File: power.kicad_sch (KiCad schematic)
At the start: 17 parts, among them Q3 AO3401A, SW2 SW_On_Off, U1 MCP73831-2-MC, U3 TPS61200DRC

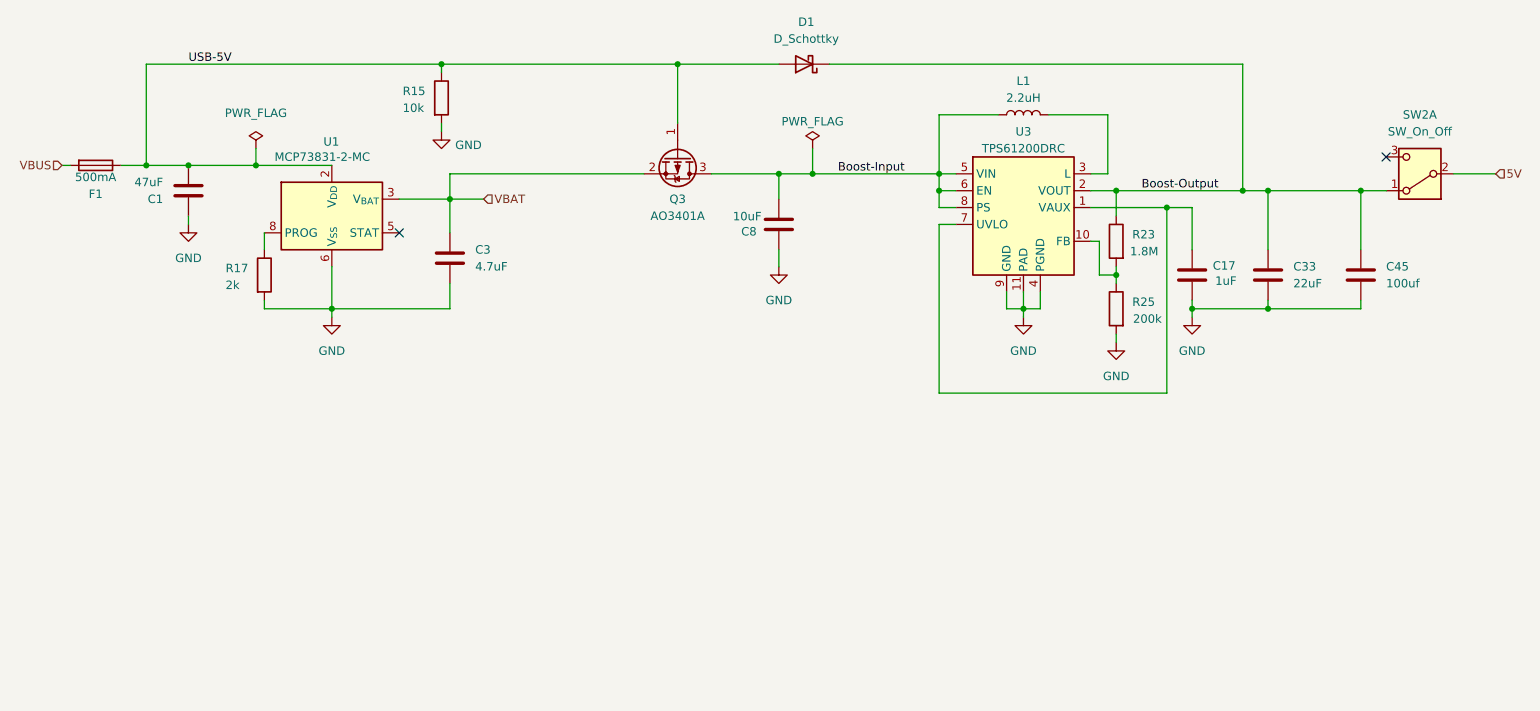
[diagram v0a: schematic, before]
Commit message: switched oout led footprint
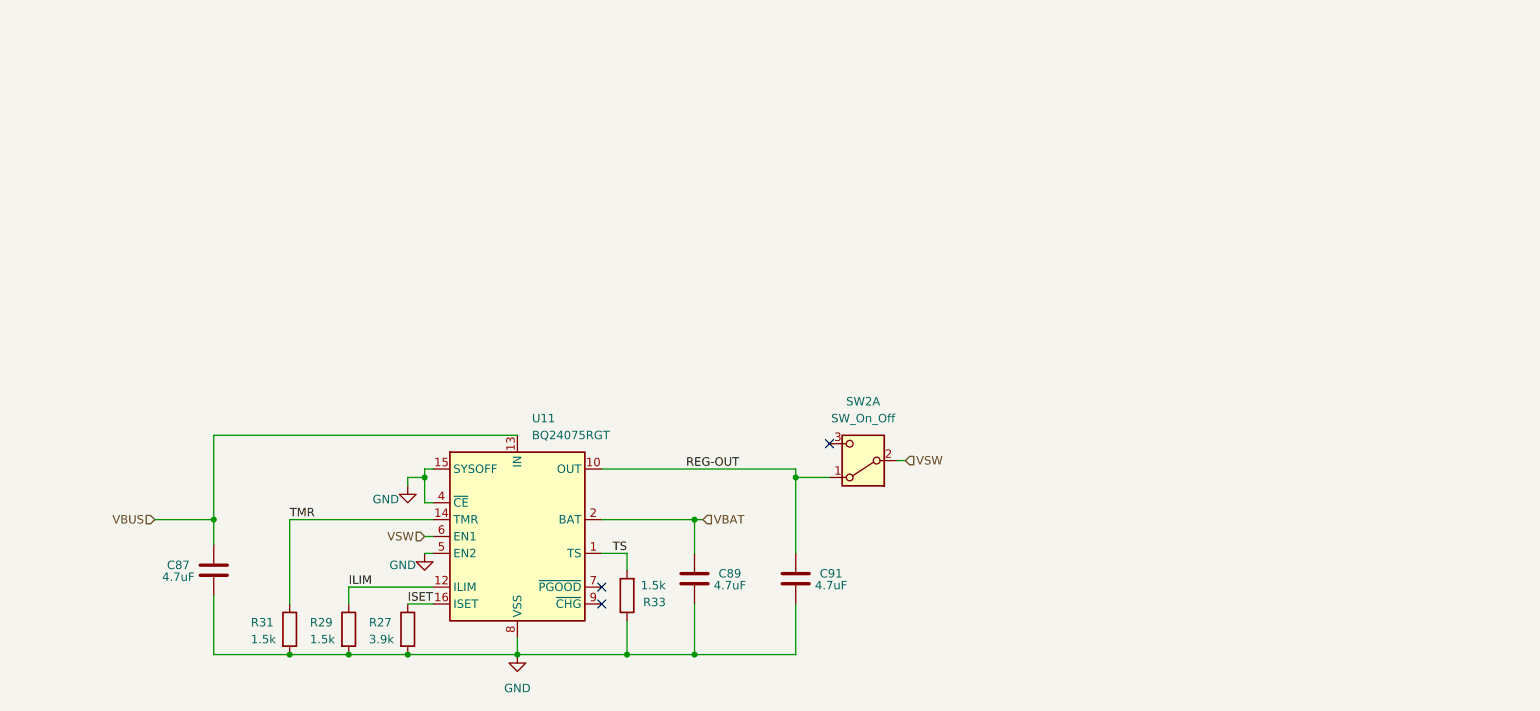
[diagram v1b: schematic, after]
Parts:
- removed C1: 47uF, Capacitor_SMD:C_0603_1608Metric, symbol Device:C
- removed C17: 1uF, Capacitor_SMD:C_0402_1005Metric, symbol Device:C
- removed C3: 4.7uF, Capacitor_SMD:C_0603_1608Metric, symbol Device:C
- removed C33: 22uF, Capacitor_SMD:C_0603_1608Metric, symbol Device:C
- removed C45: 100uf, Capacitor_SMD:C_0805_2012Metric, symbol Device:C
- removed C8: 10uF, Capacitor_SMD:C_0603_1608Metric, symbol Device:C
- removed D1: D_Schottky, Diode_SMD:D_SOD-123, symbol Device:D_Schottky
- removed F1: 500mA, Fuse:Fuse_0603_1608Metric, symbol Device:Fuse
- removed L1: 2.2uH, LPS3015-222MRC:IND_LPS3015-222MRC, symbol Device:L
- removed Q3: AO3401A, Package_TO_SOT_SMD:SOT-23, symbol Transistor_FET:AO3401A
- removed R15: 10k, Resistor_SMD:R_0402_1005Metric, symbol Device:R
- removed R17: 2k, Resistor_SMD:R_0402_1005Metric, symbol Device:R
- removed R23: 1.8M, Resistor_SMD:R_0402_1005Metric, symbol Device:R
- removed R25: 200k, Resistor_SMD:R_0402_1005Metric, symbol Device:R
- removed U1: MCP73831-2-MC, Package_DFN_QFN:DFN-8-1EP_3x2mm_P0.5mm_EP1.7x1.4mm, symbol Battery_Management:MCP73831-2-MC
- removed U3: TPS61200DRC, Package_SON:Texas_S-PVSON-N10_ThermalVias, symbol Regulator_Switching:TPS61200DRC
- added C87, C89, C91: 4.7uF, Capacitor_SMD:C_0402_1005Metric, symbol Device:C
- added R27: 3.9k, Resistor_SMD:R_0402_1005Metric, symbol Device:R
- added R29, R31, R33: 1.5k, Resistor_SMD:R_0402_1005Metric, symbol Device:R
- added U11: BQ24075RGT, Package_DFN_QFN:VQFN-16-1EP_3x3mm_P0.5mm_EP1.6x1.6mm, symbol Battery_Management:BQ24075RGT
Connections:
- net GND: now also C87.1, C89.1, C91.1, R27.2, R29.2, R31.2, R33.1, U11.15 (SYSOFF), U11.17 (VSS), U11.4 (~{CE}), U11.5 (EN2), U11.8 (VSS)
- net VBAT: now also C89.2, U11.2 (BAT), U11.3 (BAT)
- net VBUS: now also C87.2, U11.13 (IN)
- net 5V renamed VSW
- net VSW: now also U11.6 (EN1)
- net Boost-Output renamed REG-OUT
- net REG-OUT: now also C91.2, U11.10 (OUT), U11.11 (OUT)
- new net ILIM: R29.1, U11.12 (ILIM)
- new net ISET: R27.1, U11.16 (ISET)
- new net TMR: R31.1, U11.14 (TMR)
- new net TS: R33.2, U11.1 (TS)
- no-connect marks 2 -> 3
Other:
- moved on the sheet: SW2A

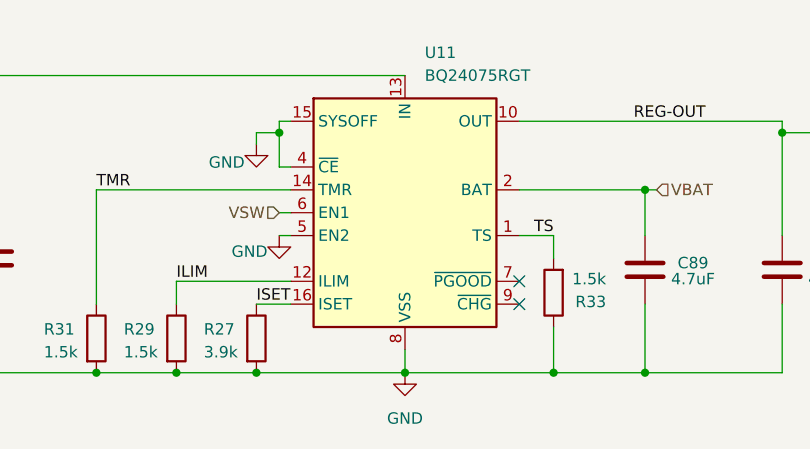
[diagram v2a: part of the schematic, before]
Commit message: added lcsc part numbers
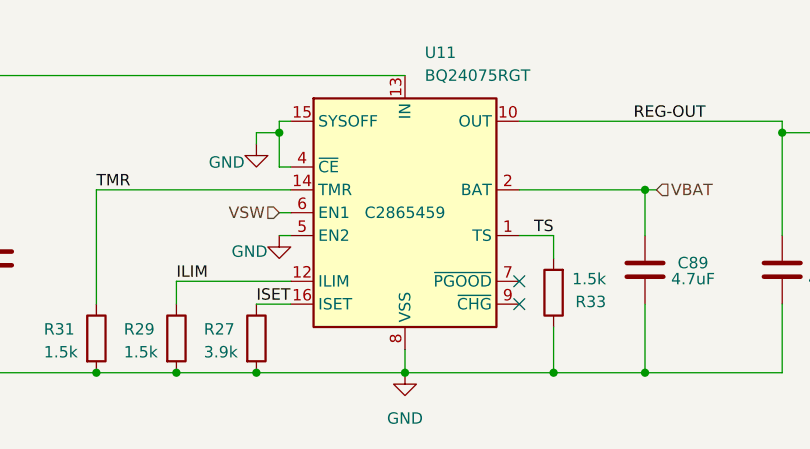
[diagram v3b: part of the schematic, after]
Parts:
- C87, C89, C91: LCSC (none) -> C307423
- R27: LCSC (none) -> C131467
- R29, R31, R33: LCSC (none) -> C25867
- U11: LCSC (none) -> C2865459
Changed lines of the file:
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@@
+			)
+		)
+		(property "LCSC" "C2865459"
+			(at 105.41 144.78 0)
+			(effects
+				(font
+					(size 1.27 1.27)
+				)
 			)
 		)
@@
 			)
 		)
+		(property "LCSC" "C307423"
+			(at 147.32 151.13 0)
+			(effects
+				(font
+					(size 1.27 1.27)
+				)
+				(hide yes)
+			)
+		)
 		(pin "1"
 		)
@@
 			)
 		)
+		(property "LCSC" "C25867"
+			(at 80.01 158.75 0)
+			(effects
+				(font
+					(size 1.27 1.27)
+				)
+				(hide yes)
+			)
+		)
 		(pin "2"
 		)
@@
 		)
 		(property "Description" "Resistor"
+			(at 71.12 158.75 0)
+			(effects
+				(font
+					(size 1.27 1.27)
+				)
+				(hide yes)
+			)
+		)
+		(property "LCSC" "C25867"
 			(at 71.12 158.75 0)
 			(effects
@@
 			)
 		)
+		(property "LCSC" "C307423"
+			(at 132.08 151.13 0)
+			(effects
+				(font
+					(size 1.27 1.27)
+				)
+				(hide yes)
+			)
+		)
 		(pin "1"
 		)
@@
 		)
 		(property "Description" "Resistor"
+			(at 88.9 158.75 0)
+			(effects
+				(font
+					(size 1.27 1.27)
+				)
+				(hide yes)
+			)
+		)
+		(property "LCSC" "C131467"
 			(at 88.9 158.75 0)
 			(effects
@@
 			)
 		)
+		(property "LCSC" "C307423"
+			(at 59.69 149.86 0)
+			(effects
+				(font
+					(size 1.27 1.27)
+				)
+				(hide yes)
+			)
+		)
 		(pin "1"
 		)
@@
 			(at 121.92 153.67 0)
 			(effects
+				(font
+					(size 1.27 1.27)
+				)
+				(hide yes)
+			)
+		)
+		(property "LCSC" "C25867"
+			(at 121.92 153.67 0)
+			(effects

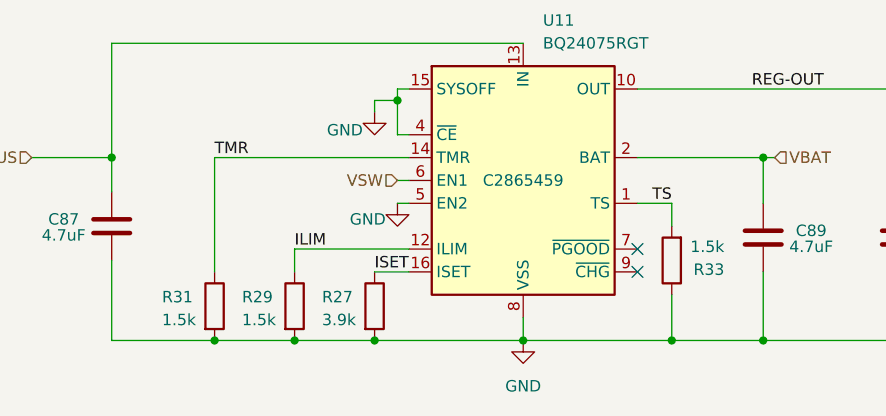
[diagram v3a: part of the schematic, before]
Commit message: checked schematic again, fixed bugs
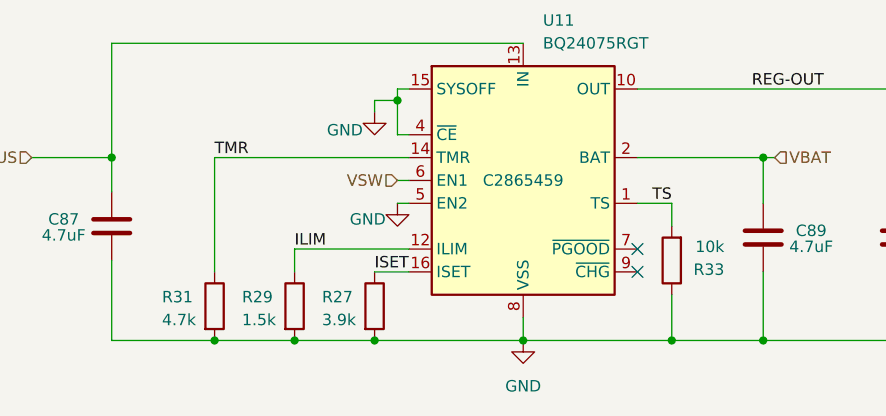
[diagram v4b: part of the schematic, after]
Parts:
- R31: value 1.5k -> 4.7k; LCSC C25867 -> C25940
- R33: value 1.5k -> 10k; LCSC C25867 -> C25744
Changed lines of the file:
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@@
 			)
 		)
-		(property "Value" "1.5k"
+		(property "Value" "4.7k"
 			(at 65.278 160.274 0)
 			(effects
@@
 			)
 		)
-		(property "LCSC" "C25867"
+		(property "LCSC" "C25940"
 			(at 71.12 158.75 0)
 			(effects
@@
 			)
 		)
-		(property "Value" "1.5k"
+		(property "Value" "10k"
 			(at 127.762 152.146 0)
 			(effects
@@
 			)
 		)
-		(property "LCSC" "C25867"
+		(property "LCSC" "C25744"
 			(at 121.92 153.67 0)
 			(effects

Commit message: new kicad version, added lcsc for the on/of switch
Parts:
- SW2: LCSC (none) -> C221662
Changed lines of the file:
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@@
 (kicad_sch
-	(version 20241209)
+	(version 20250114)
 	(generator "eeschema")
-	(generator_version "8.99")
+	(generator_version "9.0")
 	(paper "A4")
 	(junction
@@
 			(at 157.48 133.35 0)
 			(effects
+				(font
+					(size 1.27 1.27)
+				)
+				(hide yes)
+			)
+		)
+		(property "LCSC" "C221662"
+			(at 157.48 133.35 0)
+			(effects

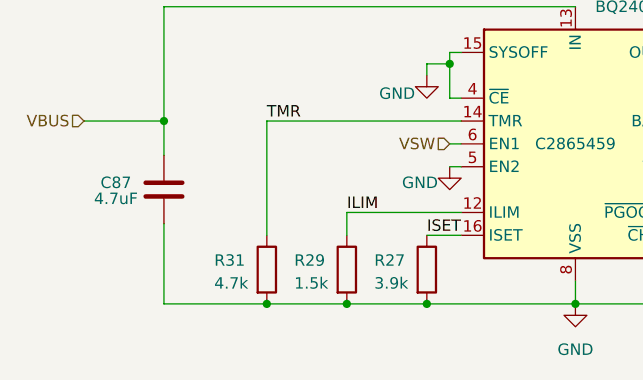
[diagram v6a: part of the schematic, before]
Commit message: fixed wrong resistor value for power management chip
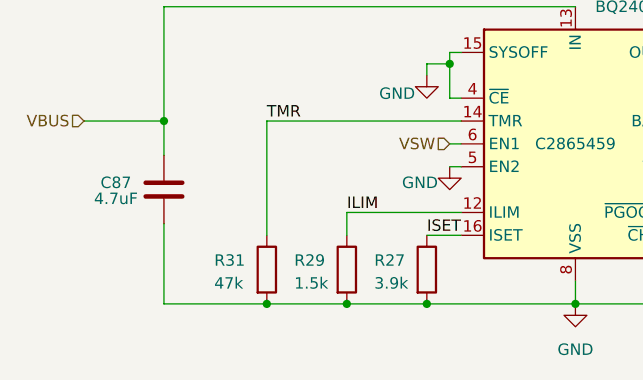
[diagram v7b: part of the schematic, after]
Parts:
- R31: value 4.7k -> 47k; LCSC C25940 -> C93943
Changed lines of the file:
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@@
 			)
 		)
-		(property "Value" "4.7k"
+		(property "Value" "47k"
 			(at 65.278 160.274 0)
 			(effects
@@
 			)
 		)
-		(property "LCSC" "C25940"
+		(property "LCSC" " C93943"
 			(at 71.12 158.75 0)
 			(effects
